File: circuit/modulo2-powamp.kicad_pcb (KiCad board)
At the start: 2 copper layers, 105 x 47 mm, 74 parts, among them J1 HOLE, J2 HOLE, J3 HOLE, J4 HOLE, J5 CONN_01X04, J6 POWER, SW1 reset, SW2 mute, SW3 HEAD/AD, U1 LM1117-5.0, U2 TPA3220, U3 MCP16331, U4 GAINSEL

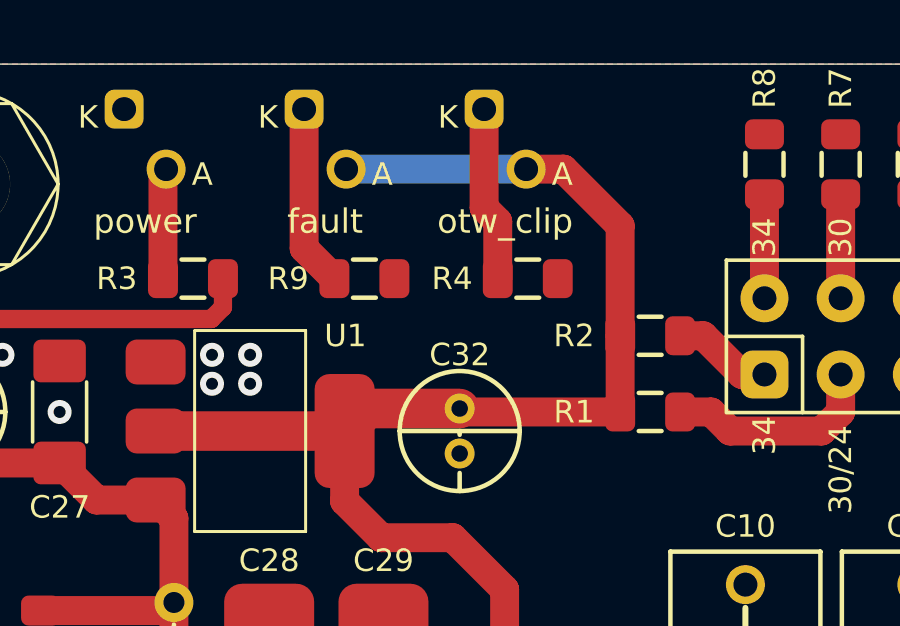
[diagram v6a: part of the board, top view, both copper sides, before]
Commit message: further routing of FV-1
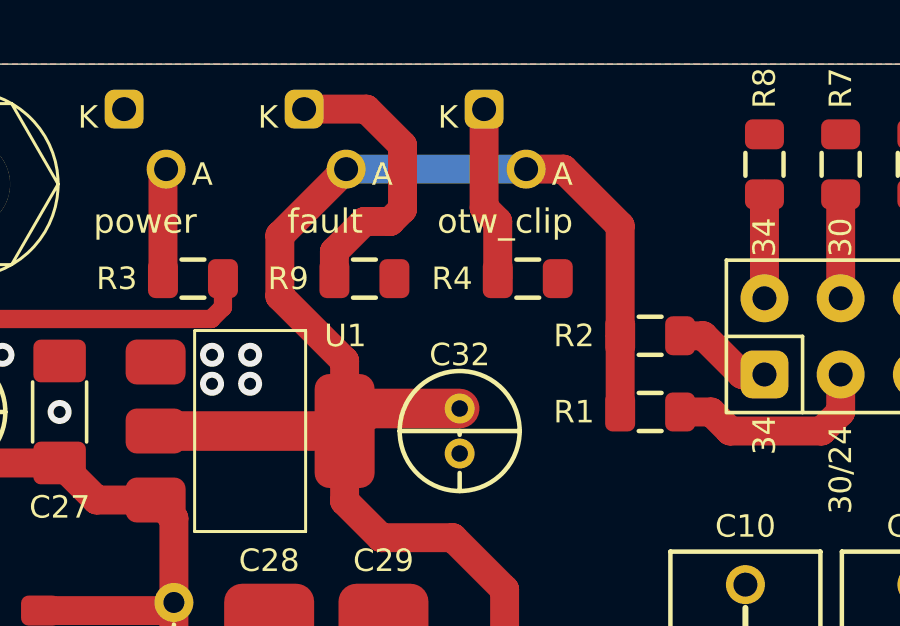
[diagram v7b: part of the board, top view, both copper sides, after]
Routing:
- net +5V: track 71.2 -> 76.4 mm
- net Net-(D3-Pad1): track 6.07 -> 9.67 mm
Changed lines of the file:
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@@
   (segment (start 75.835 59.055) (end 75.835 61.595) (width 0.9652) (layer "F.Cu") (net 3))
   (segment (start 67.81 93) (end 68.2392 93) (width 0.9652) (layer "F.Cu") (net 3))
+  (segment (start 66.7 53.5) (end 64.4906 55.7094) (width 0.9652) (layer "F.Cu") (net 3))
   (segment (start 105.47 66.9925) (end 105.47 64.28) (width 0.3048) (layer "F.Cu") (net 3))
-  (segment (start 75.835 61.595) (end 70.6 61.595) (width 0.9652) (layer "F.Cu") (net 3))
+  (segment (start 64.4906 55.7094) (end 64.4906 57.7342) (width 0.9652) (layer "F.Cu") (net 3))
   (segment (start 72.7 53.5) (end 73.947 53.5) (width 0.9652) (layer "F.Cu") (net 3))
+  (segment (start 64.4906 57.7342) (end 66.65 59.8936) (width 0.9652) (layer "F.Cu") (net 3))
   (segment (start 73.947 53.5) (end 75.835 55.388) (width 0.9652) (layer "F.Cu") (net 3))
   (segment (start 70.485 61.48) (end 67.4 61.48) (width 1.3208) (layer "F.Cu") (net 3))
-  (segment (start 70.6 61.595) (end 70.485 61.48) (width 0.9652) (layer "F.Cu") (net 3))
   (segment (start 67.4 61.48) (end 66.65 62.23) (width 1.3208) (layer "F.Cu") (net 3))
+  (segment (start 66.65 59.8936) (end 66.65 62.23) (width 0.9652) (layer "F.Cu") (net 3))
   (segment (start 66.65 64.5672) (end 66.65 62.23) (width 0.9652) (layer "F.Cu") (net 3))
   (segment (start 60.35 62.23) (end 66.65 62.23) (width 1.3208) (layer "F.Cu") (net 3))
@@
   (segment (start 71.3 51.5) (end 71.3 54.79) (width 0.9652) (layer "F.Cu") (net 19))
   (segment (start 71.3 54.79) (end 71.755 55.245) (width 0.9652) (layer "F.Cu") (net 19))
-  (segment (start 65.3 51.5) (end 65.3 56.14) (width 0.9652) (layer "F.Cu") (net 20))
-  (segment (start 65.3 56.14) (end 66.31 57.15) (width 0.9652) (layer "F.Cu") (net 20))
+  (segment (start 68.170416 55.245) (end 67.31 55.245) (width 0.9652) (layer "F.Cu") (net 20))
+  (segment (start 65.3 51.5) (end 67.375 51.5) (width 0.9652) (layer "F.Cu") (net 20))
+  (segment (start 68.58 52.705) (end 68.58 54.835416) (width 0.9652) (layer "F.Cu") (net 20))
+  (segment (start 67.375 51.5) (end 68.58 52.705) (width 0.9652) (layer "F.Cu") (net 20))
+  (segment (start 67.31 55.245) (end 66.31 56.245) (width 0.9652) (layer "F.Cu") (net 20))
+  (segment (start 68.58 54.835416) (end 68.170416 55.245) (width 0.9652) (layer "F.Cu") (net 20))
+  (segment (start 66.31 56.245) (end 66.31 57.15) (width 0.9652) (layer "F.Cu") (net 20))
   (segment (start 53.975 71.755) (end 53.975 70.215) (width 0.6096) (layer "F.Cu") (net 23))
   (segment (start 54.297202 72.077202) (end 53.975 71.755) (width 0.6096) (layer "F.Cu") (net 23))

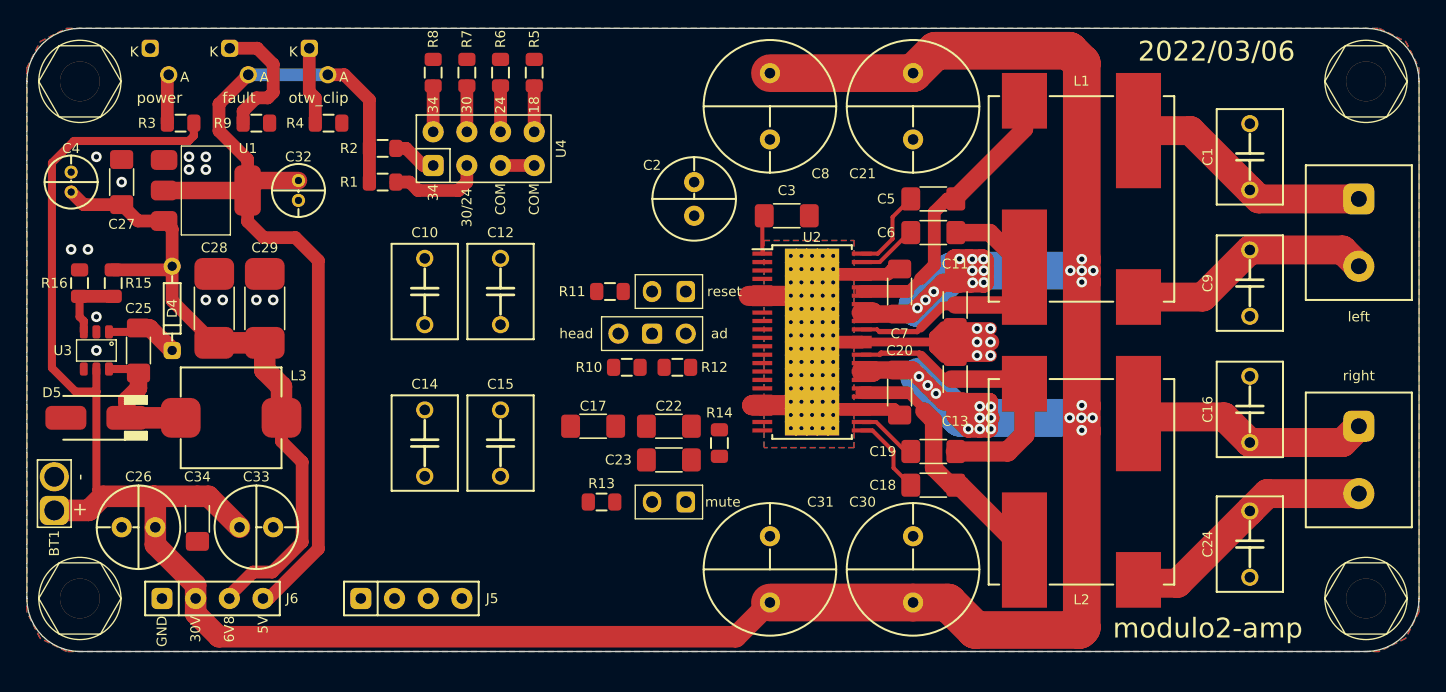
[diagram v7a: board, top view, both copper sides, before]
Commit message: no more assembler; more routing
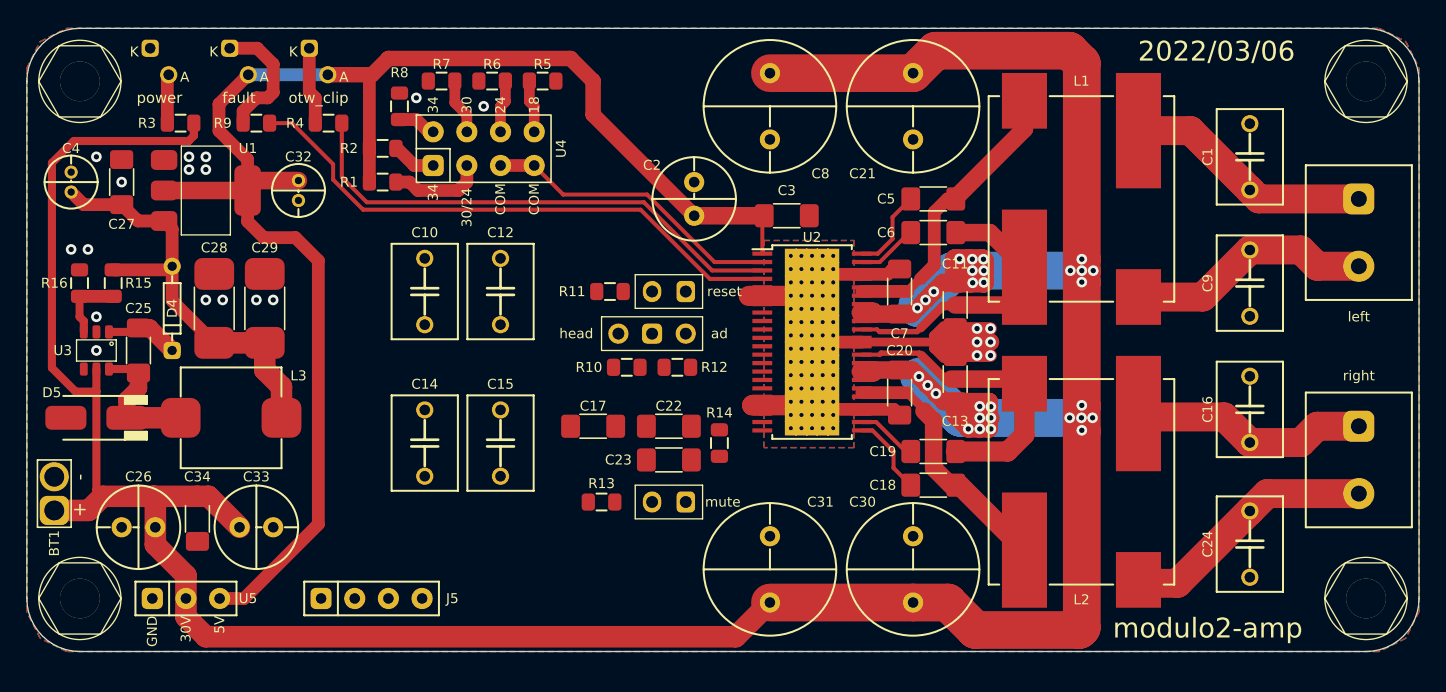
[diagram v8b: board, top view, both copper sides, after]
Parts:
- removed J6: POWER, myAmp:POWER
- added U5: POWER, myAmp:PWR_CONN, F.Cu at (62.0, 93.0)
- moved R8 3.59 mm to (78.1, 55.9)
- moved J5 3.00 mm to (76.0, 93.0)
- moved R7 2.01 mm to (81.3, 54.0), turned to 180 degrees
- moved R5 0.90 mm to (88.9, 54.0), turned to 0 degrees
- moved R6 0.90 mm to (85.1, 54.0), turned to 180 degrees
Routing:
- net FAULT: track 0.00 -> 42.7 mm
- net +5V: track 76.4 -> 116.4 mm
- net OTW_CLIP: track 0.00 -> 38.7 mm
- net Net-(U2-Pad2): track 2.54 -> 22.8 mm
- net 6V8: track 50.6 -> 33.2 mm
- net Net-(R7-Pad1): track 3.46 -> 4.20 mm
- net +BATT: track 273.7 -> 274.3 mm
- net Net-(R8-Pad1): track 3.46 -> 2.92 mm
- net Net-(R6-Pad1): track 3.46 -> 3.98 mm
- net Net-(R5-Pad1): track 3.46 -> 3.98 mm
- net GND: vias 20 -> 22
